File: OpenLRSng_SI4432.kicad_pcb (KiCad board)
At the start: 2 copper layers, 22 x 40.6 mm, 33 parts, among them IC1 ATMEGA328P-A, IC2 Si4432, P1 CONN_01X06, P2 CONN_02X06, P3 MML, U1 MIC5205 3,3V, Y1 RESONATEUR

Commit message: 100uF Cap von 1206 auf 1210 geändert
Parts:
- C12: footprint Capacitors_SMD:C_1206 -> Capacitors_SMD:C_1210
- C2: value 100µ -> 22u

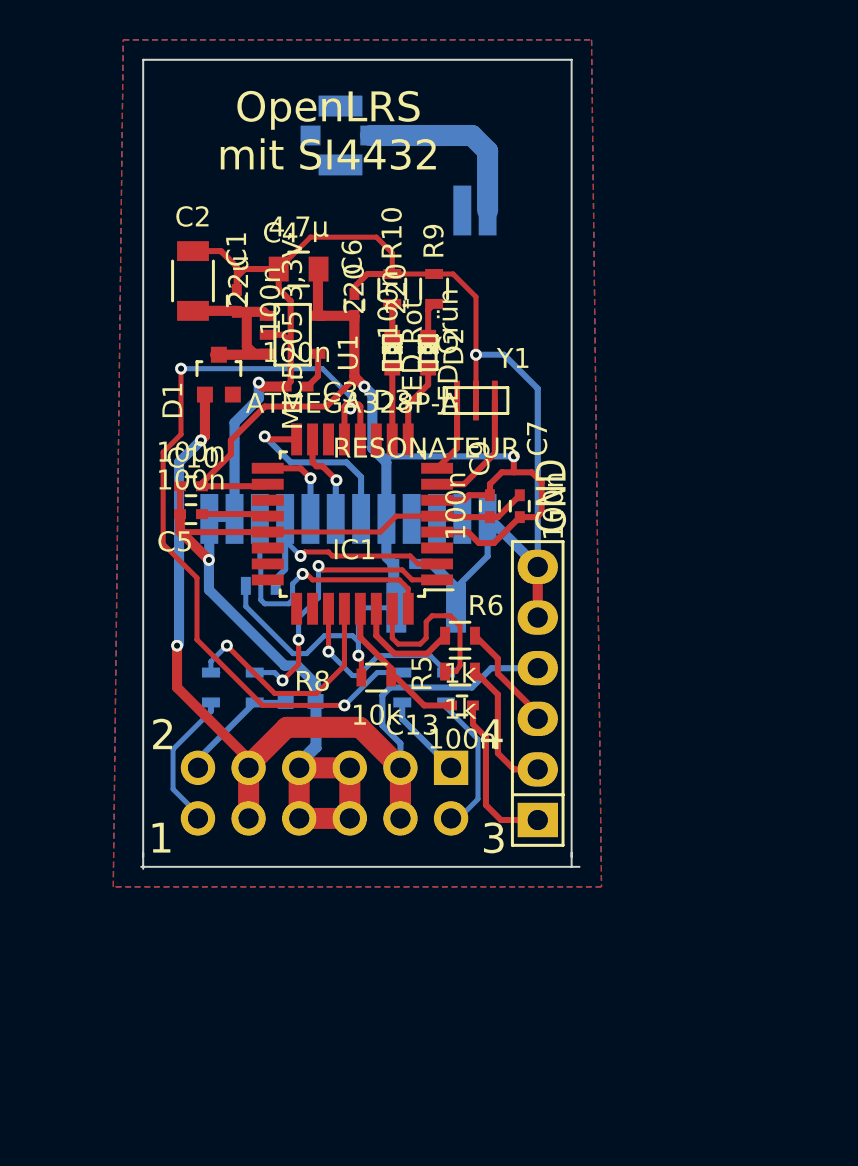
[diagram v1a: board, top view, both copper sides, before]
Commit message: -SI4432 Bibliothek gefixt (Pin14 GND vergessen im Schaltplan) -DuKo Kupferfläche vergrößert -zusätzlich noch einmal 100uF Kerko an die 3,3V Rail -Via Stichting an der Massefläche
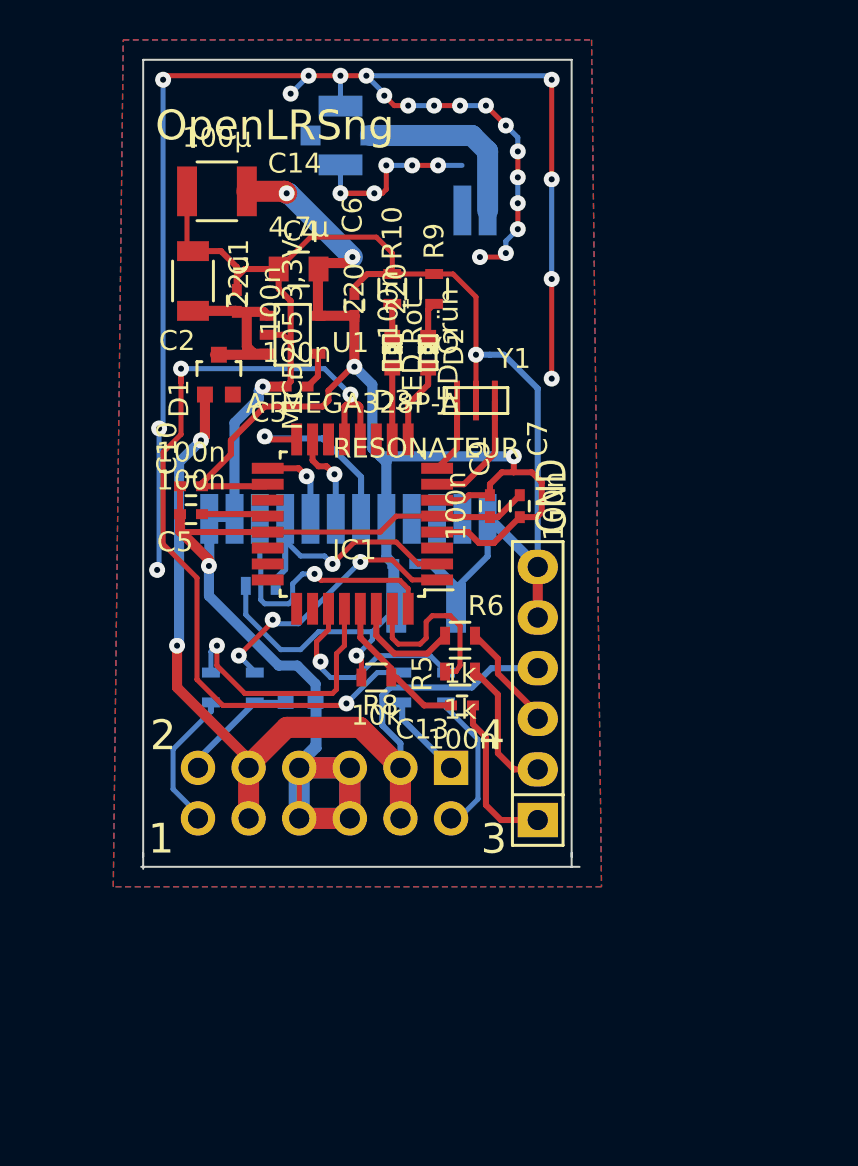
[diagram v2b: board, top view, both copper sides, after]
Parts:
- added C14: 100µ, Capacitors_SMD:C_1210, F.Cu at (200.7, 57.6)
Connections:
- IC2 pad 14: (no net) -> GND
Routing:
- net GND: track 128.7 -> 229.8 mm, vias 3 -> 31
- net +3.3V: track 85.8 -> 91.6 mm, vias 3 -> 5
- net /SCL: track 12.4 -> 13.7 mm
- net /PPM: track 41.4 -> 42.7 mm
- net /SDA: track 9.34 -> 10.6 mm
- net +5V: track 47.6 -> 48.8 mm
- net Net-(IC1-Pad16): track 9.45 -> 10.2 mm
- net Net-(IC1-Pad2): track 12.9 -> 13.7 mm
- net /RSSI: track 14.3 -> 13.8 mm
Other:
- net class Default: via_dia 0.6 -> 0.8
- rule via_min_size: 0.6 -> 0.8
- board text added: "OpenLRSng"
- board text removed: "OpenLRS mit SI4432"

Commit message: 4 Kanal auf 6 Kanal umgebaut und leicht optimiert
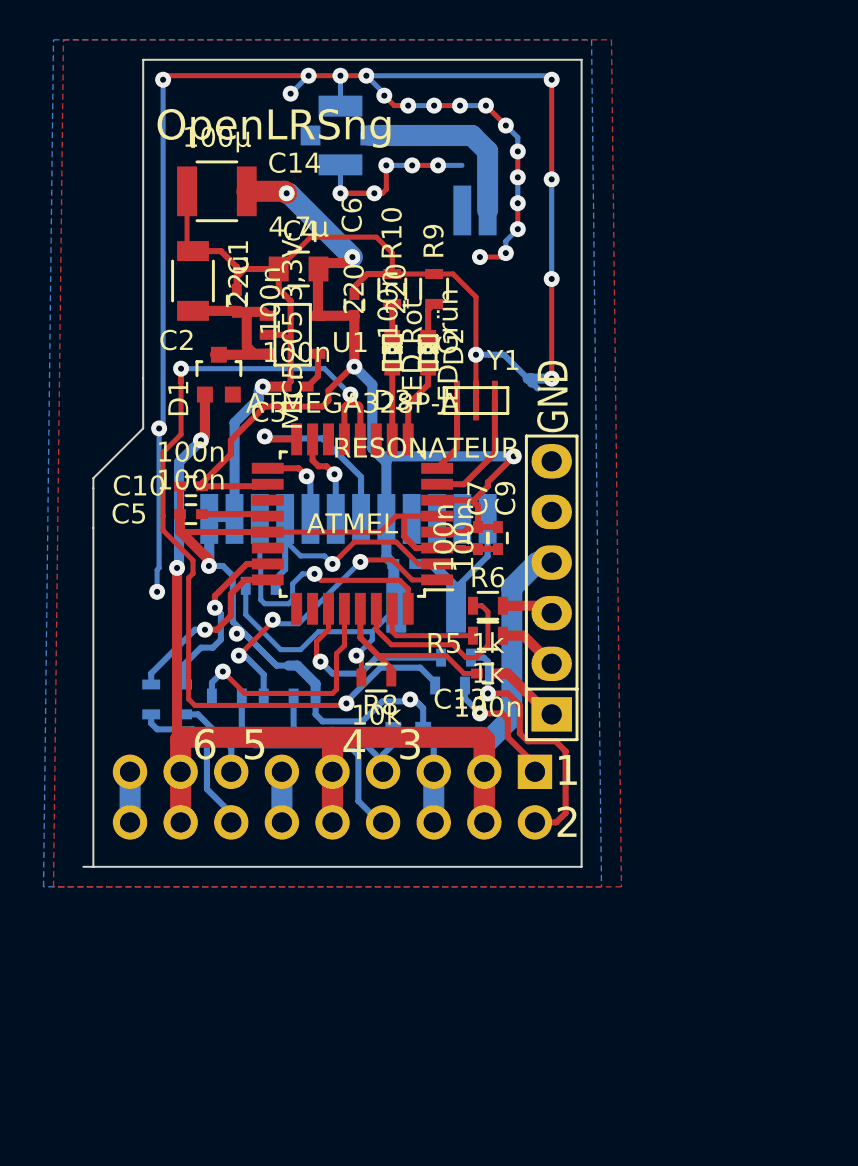
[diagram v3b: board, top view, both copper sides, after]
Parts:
- added R101: 1k, Resistors_SMD:R_0603, B.Cu at (199.0, 83.1)
- added R102: 1k, Resistors_SMD:R_0603, B.Cu at (197.4, 83.1)
- P2: value CONN_02X06 -> CONN_02X09; footprint Pin_Headers:Pin_Header_Angled_2x06 -> Pin_Headers:Pin_Header_Angled_2x09
- moved C8 5.58 mm to (210.3, 84.6)
- moved P1 5.35 mm to (217.5, 77.5)
- moved R1 2.40 mm to (212.4, 82.4), turned to 180 degrees
- moved R5 2.28 mm to (214.3, 79.9)
- moved C13 2.06 mm to (214.3, 81.8)
- moved R6 2.05 mm to (214.3, 78.4)
- moved C9 1.94 mm to (214.8, 75.0), turned to 270 degrees
- moved C7 1.71 mm to (213.8, 75.0)
- moved R3 1.58 mm to (212.7, 81.0), turned to 0 degrees
- moved R2 1.30 mm to (203.8, 83.0), turned to 180 degrees
- moved R4 0.94 mm to (201.2, 83.0), turned to 0 degrees
- moved P2 0.45 mm to (206.5, 88.0)
- renumbered IC1 to ATMEL, IC2 to SI4432
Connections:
- ATMEL pad 23: Net-(IC1-Pad23) -> /ch5
- ATMEL pad 24: Net-(IC1-Pad24) -> /ch6
- P2 pad 11: /RSSIanalog -> GND
- P2 pad 12: Net-(P2-Pad12) -> GND
- P2 pad 7: GND -> /RSSIanalog
- P2 pad 8: GND -> Net-(P2-Pad8)
- R4 pad 2: Net-(P2-Pad12) -> Net-(P2-Pad8)
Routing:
- net GND: track 229.8 -> 213.8 mm, vias 31 -> 33
- net Net-(P2-Pad8): track 0.00 -> 12.1 mm
- net +5V: track 48.8 -> 59.3 mm
- net /ch5: track 0.00 -> 9.38 mm, vias 0 -> 1
- net /ch6: track 0.00 -> 9.05 mm, vias 0 -> 1
- net Net-(P2-Pad14): track 0.00 -> 8.14 mm
- net Net-(P2-Pad12): track 7.57 -> 0.00 mm
- net Net-(P2-Pad2): track 7.31 -> 13.3 mm, vias 0 -> 1
- net /DTR: track 9.03 -> 4.14 mm
- net /RX: track 5.55 -> 10.1 mm
- net Net-(P2-Pad13): track 0.00 -> 4.32 mm
- net /TX: track 9.38 -> 5.28 mm
- net /RSSIanalog: track 5.71 -> 9.57 mm
- net Net-(P1-Pad2): track 6.91 -> 3.19 mm
- net +3.3V: track 91.6 -> 88.1 mm
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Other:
- board size 22 x 40.6 mm -> 25 x 40.5 mm
- board text added: "5"
- board text added: "6"

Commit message: picoblade dazu und layout etwas weiter. noch unfertig.
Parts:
- removed R101, R102: 1k, Resistors_SMD:R_0603
- removed SI4432: Si4432, SI4432_Module:SI4432_Module
- added C15, C16: 100n, Capacitors_SMD:C_0402, F.Cu at (206.5, 101.6)
- added IC2: Si4432, SI4432_Module:SI4432_Module, B.Cu at (207.2, 66.3)
- added P4: CONN_01X04, Connectors_Molex:Connector_Molex_PicoBlade_53398-0471, F.Cu at (196.2, 79.5)
- added R12, R14: *k, Resistors_SMD:R_0603, F.Cu at (206.5, 101.6)
- added R13: 10k, Resistors_SMD:R_0603, F.Cu at (206.5, 101.6)
- added R15: 1k, Resistors_SMD:R_0603, F.Cu at (206.5, 101.6)
- added R16: 1k, Resistors_SMD:R_0603, F.Cu at (229.1, 79.8)
- added R7: 10k, Resistors_SMD:R_0603, F.Cu at (226.2, 79.8)
- P2: value CONN_02X09 -> CONN_02X06
- renumbered ATMEL to IC1
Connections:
- IC1 pad 11: Net-(IC1-Pad11) -> (no net)
- IC1 pad 14: Net-(IC1-Pad14) -> (no net)
- IC1 pad 19: Net-(IC1-Pad19) -> (no net)
- IC1 pad 22: Net-(IC1-Pad22) -> (no net)
- IC1 pad 25: Net-(IC1-Pad25) -> (no net)
- IC1 pad 26: Net-(IC1-Pad26) -> (no net)
- P2 pad 11: GND -> /RSSIanalog
- P2 pad 12: GND -> Net-(P2-Pad12)
- P2 pad 13: Net-(P2-Pad13) -> (no net)
- P2 pad 14: Net-(P2-Pad14) -> (no net)
- P2 pad 15: +5V -> (no net)
- P2 pad 16: +5V -> (no net)
- P2 pad 17: GND -> (no net)
- P2 pad 18: GND -> (no net)
- P2 pad 7: /RSSIanalog -> GND
- P2 pad 8: Net-(P2-Pad8) -> GND
- R1 pad 1: Net-(P2-Pad1) -> /SCL
- R1 pad 2: /PPM -> Net-(P4-Pad3)
- R2 pad 1: /RSSIanalog -> /SDA
- R2 pad 2: /RSSI -> Net-(P4-Pad4)
- R3 pad 1: /SDA -> Net-(P2-Pad1)
- R3 pad 2: Net-(P2-Pad2) -> /PPM
- R4 pad 1: /SCL -> /RSSIanalog
- R4 pad 2: Net-(P2-Pad8) -> /RSSI
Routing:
- net /PPM: track 45.9 -> 4.18 mm, vias 3 -> 0
- net /RSSI: track 15.4 -> 0.00 mm, vias 3 -> 0
- net Net-(P2-Pad2): track 13.3 -> 0.01 mm, vias 1 -> 0
- net Net-(P2-Pad8): track 12.1 -> 0.00 mm
- net /SCL: track 11.7 -> 0.00 mm, vias 1 -> 0
- net /SDA: track 9.91 -> 0.00 mm, vias 1 -> 0
- net /ch5: track 9.38 -> 0.00 mm, vias 1 -> 0
- net /ch6: track 9.05 -> 0.07 mm, vias 1 -> 0
- net Net-(P2-Pad14): track 8.14 -> 0.00 mm
- net /RSSIanalog: track 9.57 -> 2.54 mm
- net Net-(P2-Pad1): track 6.43 -> 0.37 mm, vias 1 -> 0
- net GND: track 213.8 -> 209.0 mm
- net Net-(P2-Pad13): track 4.32 -> 0.00 mm
- net (no net): track 0.00 -> 2.99 mm

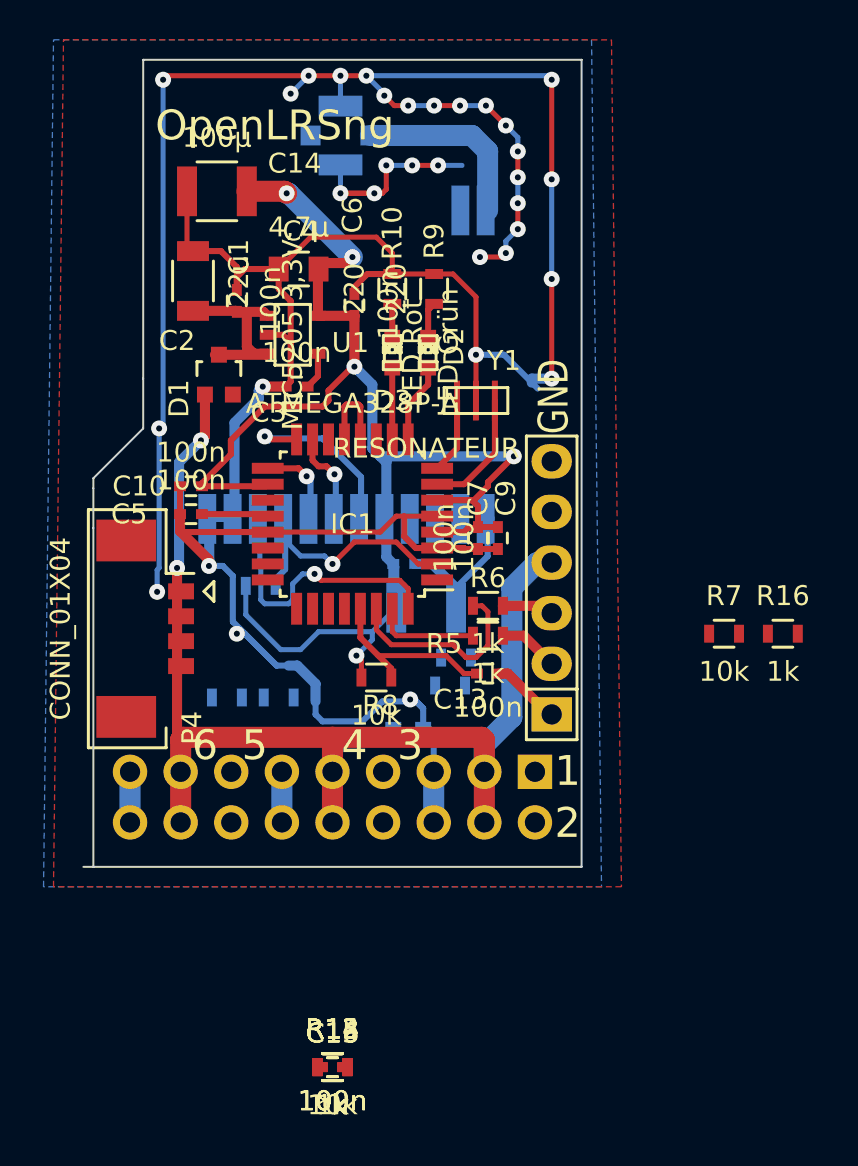
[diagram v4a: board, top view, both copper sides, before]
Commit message: I²C Stecker im APM-Layout dazugefügt und Layout soweit fertig gemacht
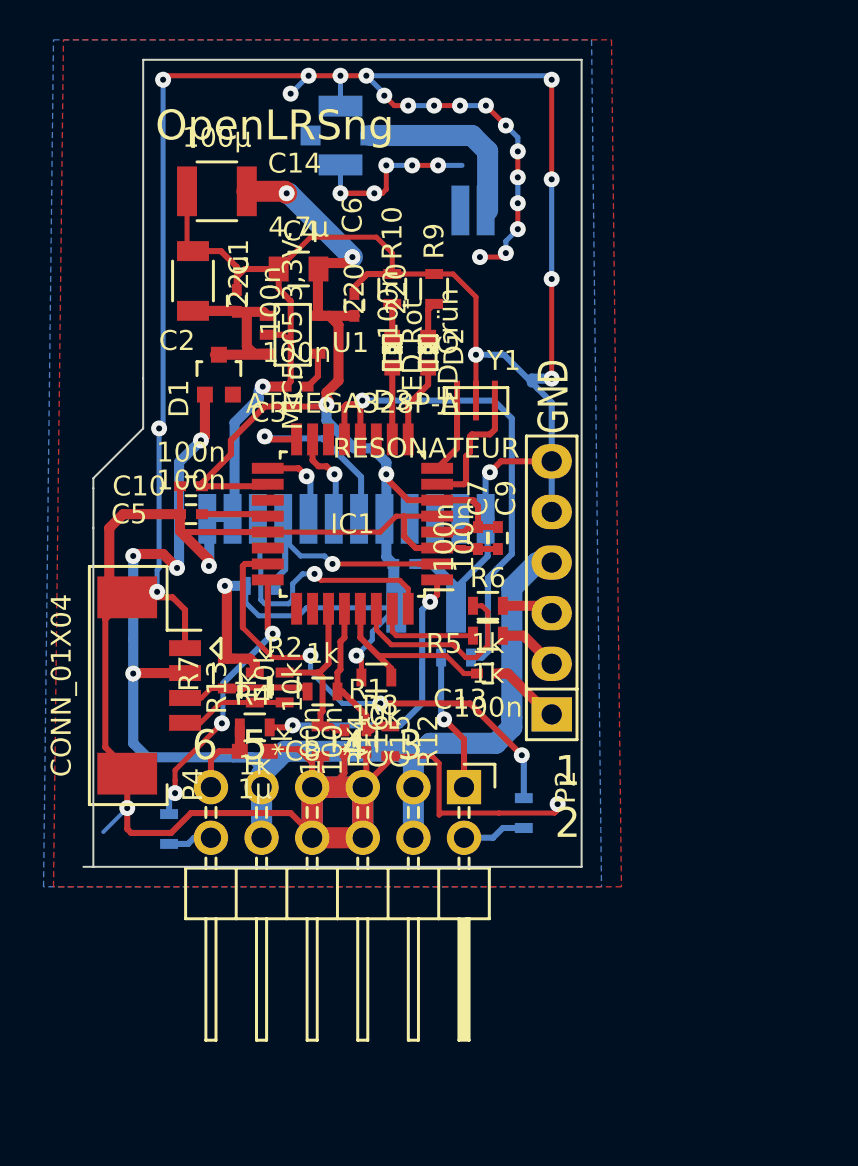
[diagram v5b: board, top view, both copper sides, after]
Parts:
- C8, R1, R2, R4: moved to F.Cu
- P2: footprint Pin_Headers:Pin_Header_Angled_2x09 -> Pin_Headers:Pin_Header_Angled_2x06
- P4: footprint Connectors_Molex:Connector_Molex_PicoBlade_53398-0471 -> Connectors_Molex:Connector_Molex_PicoBlade_53261-0471
- R15, R16: moved to B.Cu
- moved R16 32.3 mm to (198.3, 89.6), turned to 270 degrees
- moved R7 25.0 mm to (201.2, 81.8), turned to 90 degrees
- moved R13 19.4 mm to (202.6, 82.5), turned to 90 degrees
- moved R12 16.6 mm to (209.4, 85.2), turned to 270 degrees
- moved C15 16.4 mm to (208.2, 85.2), turned to 270 degrees
- moved C16 16.4 mm to (207.1, 85.2), turned to 270 degrees
- moved R14 16.4 mm to (205.9, 85.2), turned to 270 degrees
- moved R15 16.0 mm to (216.1, 88.8), turned to 270 degrees
- moved C8 7.78 mm to (202.6, 85.7)
- moved P2 6.62 mm to (213.1, 87.5), turned to 270 degrees
- moved R1 6.41 mm to (206.0, 82.7)
- moved P4 2.85 mm to (196.2, 82.4)
- moved R4 2.05 mm to (202.6, 84.5)
- moved R2 0.58 mm to (204.1, 82.5), turned to 270 degrees
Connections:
- IC1 pad 11: (no net) -> Net-(IC1-Pad11)
- IC1 pad 14: (no net) -> Net-(IC1-Pad14)
- IC1 pad 19: (no net) -> Net-(IC1-Pad19)
- IC1 pad 22: (no net) -> Net-(IC1-Pad22)
- IC1 pad 25: (no net) -> Net-(IC1-Pad25)
- IC1 pad 26: (no net) -> Net-(IC1-Pad26)
- IC2 pad 2: (no net) -> Net-(IC2-Pad2)
- IC2 pad 3: (no net) -> Net-(IC2-Pad3)
- IC2 pad 4: (no net) -> Net-(IC2-Pad4)
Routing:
- net GND: track 209.0 -> 275.6 mm, vias 33 -> 34
- net /ch5: track 0.00 -> 23.8 mm, vias 0 -> 3
- net /PPM: track 4.18 -> 25.8 mm, vias 0 -> 1
- net /RSSI: track 0.00 -> 14.7 mm, vias 0 -> 2
- net /ch6: track 0.07 -> 14.7 mm, vias 0 -> 3
- net /SDA: track 0.00 -> 9.26 mm
- net /SCL: track 0.00 -> 8.27 mm
- net +5V: track 59.3 -> 66.3 mm, vias 2 -> 4
- net Net-(P2-Pad1): track 0.37 -> 6.98 mm, vias 0 -> 1
- net Net-(P4-Pad3): track 0.15 -> 6.45 mm
- net Net-(P4-Pad4): track 0.00 -> 6.00 mm
- net +3.3V: track 88.1 -> 82.6 mm, vias 5 -> 6
- net Net-(P2-Pad2): track 0.01 -> 3.20 mm
- net (no net): track 2.99 -> 0.00 mm
- net Net-(P2-Pad12): track 0.00 -> 2.23 mm
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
